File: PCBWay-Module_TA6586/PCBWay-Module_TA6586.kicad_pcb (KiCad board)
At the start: 2 copper layers, 16.3 x 21.2 mm, 4 parts, among them J1 Conn_01x07_Pin, J2 Conn_01x07_Pin

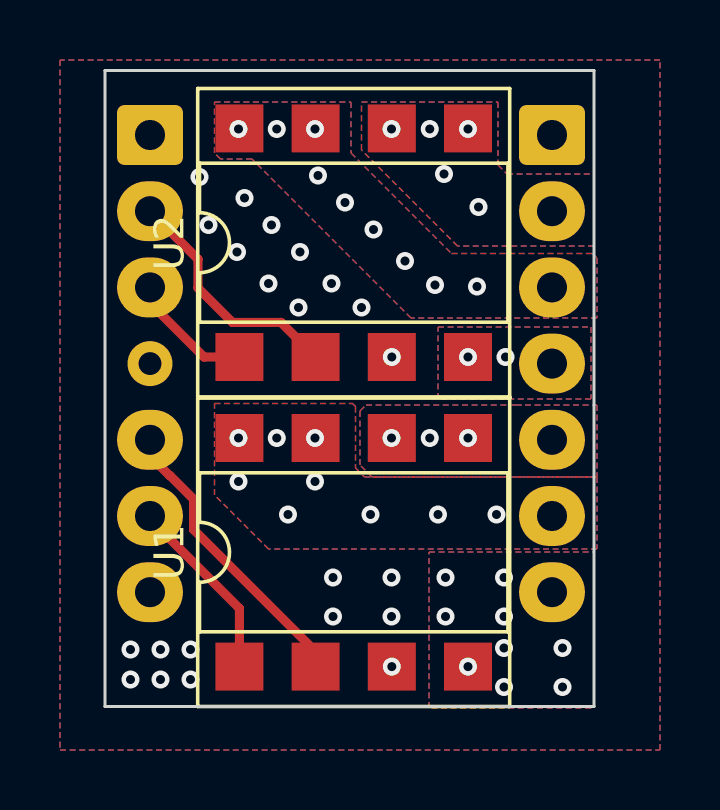
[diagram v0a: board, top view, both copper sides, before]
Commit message: Added capacitors
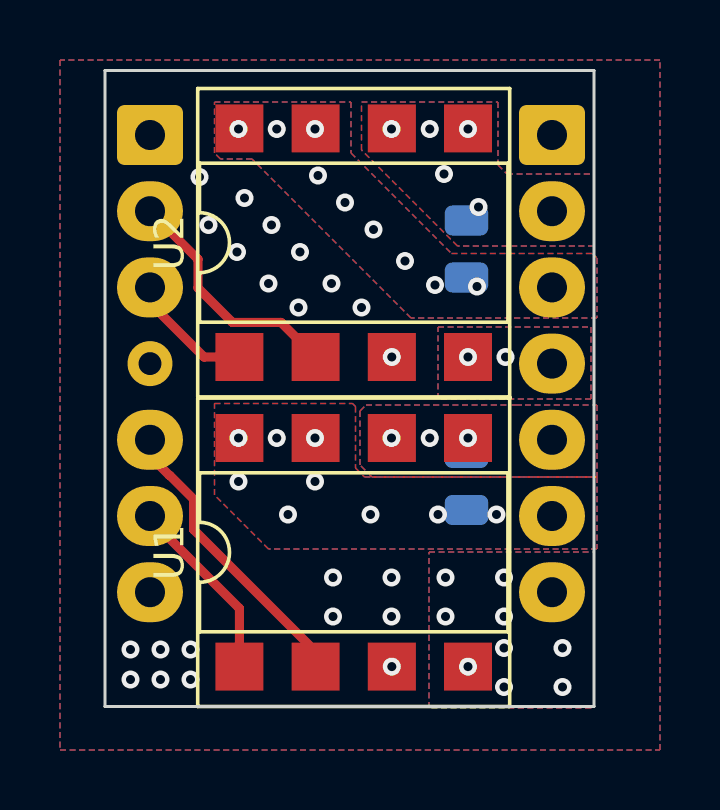
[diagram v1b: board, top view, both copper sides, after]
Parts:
- added C1: 100, Capacitor_SMD:C_0805_2012Metric, B.Cu at (150.6, 73.3)
- added C2: 100, Capacitor_SMD:C_0805_2012Metric, B.Cu at (150.6, 81.0)
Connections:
- J1 pad 4: (no net) -> unconnected-(J1-Pin_4-Pad4)
